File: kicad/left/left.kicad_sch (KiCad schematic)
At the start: 48 parts, among them J1 59453-121110ECHLF, J2 59453-051110ECHLF, J3 59453-051110ECHLF, J4 59453-081110EDHLF, J5 59453-081110EDHLF, U1 RP2040_Zero

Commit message: break up parts
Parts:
- removed D19, D20, D21, D22, D23, D24, D27, D28, D29, D30: D, ScottoKeebs_Components:Diode_SOD-123, symbol Device:D
- removed H4, H5: Mounting_Hole, MountingHole:MountingHole_2.2mm_M2_Pad_Via, symbol ScottoKeebs:Placeholder_Mounting_Hole
- removed J3: 59453-051110ECHLF, AMPHENOL_59453-051110ECHLF, symbol 59453-051110ECHLF:59453-051110ECHLF
- removed J4: 59453-081110EDHLF, AMPHENOL_59453-081110EDHLF, symbol 59453-081110EDHLF:59453-081110EDHLF
- removed S5, S6: SKRHADE010, SKRHADE010, symbol SKRHADE010:SKRHADE010
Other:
- moved on the sheet: H1, H2, H3, J1, J2, J5

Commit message: wiring
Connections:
- net GND: now also J2.5; no longer J2.4
- net JC: now also J2.4; no longer J2.3
- net JX: now also J2.3; no longer J2.5

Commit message: Add connectors
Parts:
- added J3: Conn_01x06_Pin, footprints:Pointing-connector, symbol Connector:Conn_01x06_Pin
- added J4: Conn_01x05_Pin, footprints:Joystick-connector, symbol Connector:Conn_01x05_Pin
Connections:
- net 3V3: now also J3.6 (Pin_6), J4.5 (Pin_5)
- net GND: now also J3.5 (Pin_5), J4.1 (Pin_1)
- net JC: now also J4.2 (Pin_2)
- net JX: now also J4.3 (Pin_3)
- net JY: now also J4.4 (Pin_4)
- net MISO: now also J3.2 (Pin_2)
- net MOSI: now also J3.4 (Pin_4)
- net SCK: now also J3.1 (Pin_1)
- net SS: now also J3.3 (Pin_3)

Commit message: Update footprints
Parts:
- H1, H2, H3: footprint MountingHole:MountingHole_2.2mm_M2_Pad_Via -> footprints:MountingHole_2.2mm_M2_Pad_Via
- J1: footprint AMPHENOL_59453-121110ECHLF -> footprints:AMPHENOL_59453-121110ECHLF
- J2: footprint AMPHENOL_59453-051110ECHLF -> footprints:AMPHENOL_59453-051110ECHLF
- J5: footprint AMPHENOL_59453-081110EDHLF -> footprints:AMPHENOL_59453-081110EDHLF
- S1, S2, S3, S4: footprint SKRHADE010 -> footprints:SKRHADE010
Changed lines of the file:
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@@
 			)
 		)
-		(property "Footprint" "SKRHADE010"
+		(property "Footprint" "footprints:SKRHADE010"
 			(at 59.69 143.18 0)
 			(effects
@@
 			)
 		)
-		(property "Footprint" "MountingHole:MountingHole_2.2mm_M2_Pad_Via"
+		(property "Footprint" "footprints:MountingHole_2.2mm_M2_Pad_Via"
 			(at 105.41 97.79 0)
 			(effects
@@
 			)
 		)
-		(property "Footprint" "SKRHADE010"
+		(property "Footprint" "footprints:SKRHADE010"
 			(at 129.54 143.18 0)
 			(effects
@@
 			)
 		)
-		(property "Footprint" "MountingHole:MountingHole_2.2mm_M2_Pad_Via"
+		(property "Footprint" "footprints:MountingHole_2.2mm_M2_Pad_Via"
 			(at 105.41 109.22 0)
 			(effects
@@
 			)
 		)
-		(property "Footprint" "SKRHADE010"
+		(property "Footprint" "footprints:SKRHADE010"
 			(at 199.39 143.18 0)
 			(effects
@@
 			)
 		)
-		(property "Footprint" "SKRHADE010"
+		(property "Footprint" "footprints:SKRHADE010"
 			(at 269.24 143.18 0)
 			(effects
@@
 			)
 		)
-		(property "Footprint" "MountingHole:MountingHole_2.2mm_M2_Pad_Via"
+		(property "Footprint" "footprints:MountingHole_2.2mm_M2_Pad_Via"
 			(at 105.41 104.14 0)
 			(effects
@@
 			)
 		)
-		(property "Footprint" "AMPHENOL_59453-051110ECHLF"
+		(property "Footprint" "footprints:AMPHENOL_59453-051110ECHLF"
 			(at 209.55 93.98 0)
 			(effects
@@
 			)
 		)
-		(property "Footprint" "AMPHENOL_59453-081110EDHLF"
+		(property "Footprint" "footprints:AMPHENOL_59453-081110EDHLF"
 			(at 254 92.71 0)
 			(effects
@@
 			)
 		)
-		(property "Footprint" "AMPHENOL_59453-121110ECHLF"
+		(property "Footprint" "footprints:AMPHENOL_59453-121110ECHLF"
 			(at 157.48 95.25 0)
 			(effects

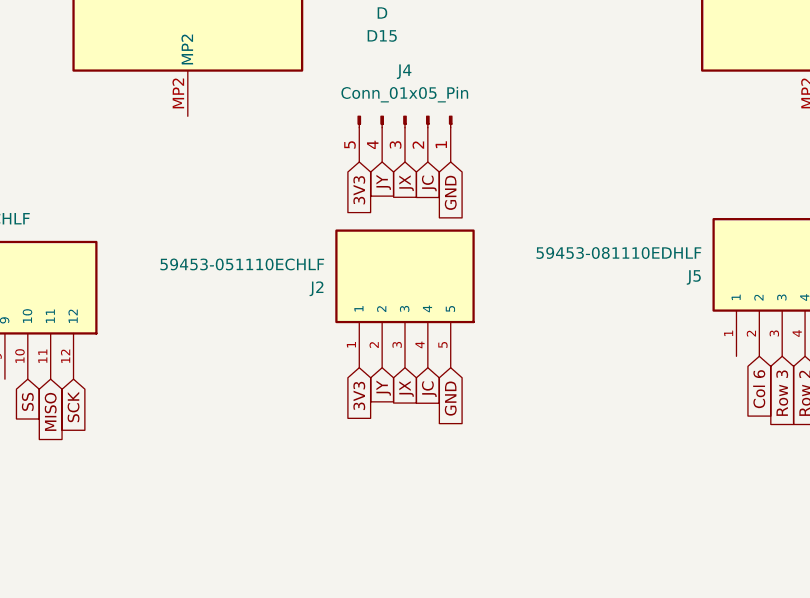
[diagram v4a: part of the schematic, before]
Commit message: Add joystick breakout
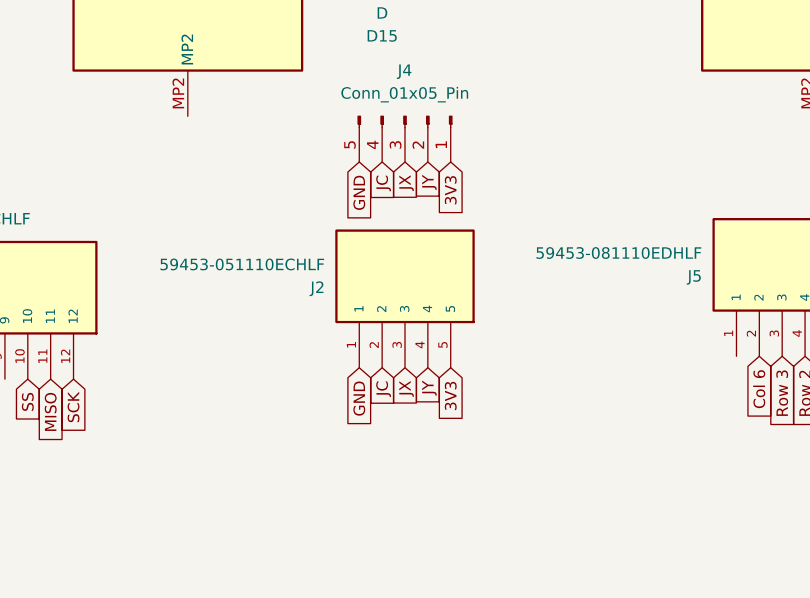
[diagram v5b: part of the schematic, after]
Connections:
- net 3V3: now also J2.5, J4.1 (Pin_1); no longer J2.1, J4.5 (Pin_5)
- net GND: now also J2.1, J4.5 (Pin_5); no longer J2.5, J4.1 (Pin_1)
- net JC: now also J2.2, J4.4 (Pin_4); no longer J2.4, J4.2 (Pin_2)
- net JY: now also J2.4, J4.2 (Pin_2); no longer J2.2, J4.4 (Pin_4)

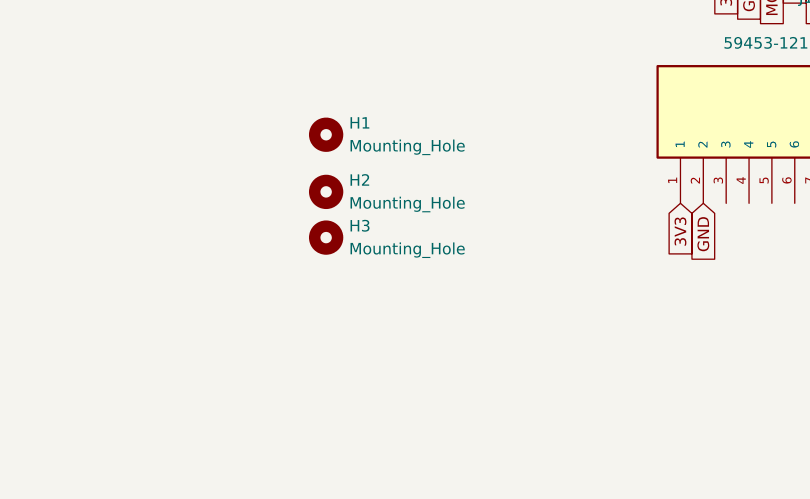
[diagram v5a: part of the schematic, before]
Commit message: Add holes
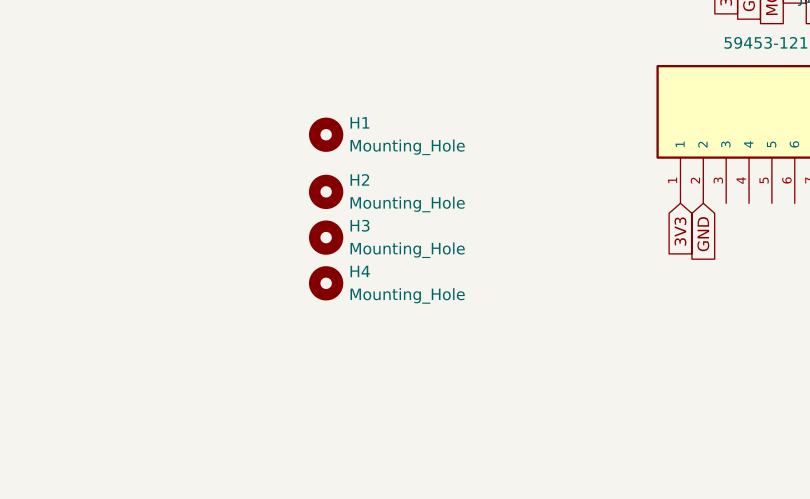
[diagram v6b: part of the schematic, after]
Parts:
- added H4: Mounting_Hole, footprints:MountingHole_2.2mm_M2_Pad_Via, symbol ScottoKeebs:Placeholder_Mounting_Hole
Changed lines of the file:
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@@
+	)
+	(symbol
+		(lib_id "ScottoKeebs:Placeholder_Mounting_Hole")
+		(at 105.41 114.3 0)
+		(unit 1)
+		(exclude_from_sim no)
+		(in_bom yes)
+		(on_board yes)
+		(dnp no)
+		(fields_autoplaced yes)
+		(property "Reference" "H4"
+			(at 107.95 113.0299 0)
+			(effects
+				(font
+					(size 1.27 1.27)
+				)
+				(justify left)
+			)
+		)
+		(property "Value" "Mounting_Hole"
+			(at 107.95 115.5699 0)
+			(effects
+				(font
+					(size 1.27 1.27)
+				)
+				(justify left)
+			)
+		)
+		(property "Footprint" "footprints:MountingHole_2.2mm_M2_Pad_Via"
+			(at 105.41 114.3 0)
+			(effects
+				(font
+					(size 1.27 1.27)
+				)
+				(hide yes)
+			)
+		)
+		(property "Datasheet" "~"
+			(at 105.41 114.3 0)
+			(effects
+				(font
+					(size 1.27 1.27)
+				)
+				(hide yes)
+			)
+		)
+		(property "Description" "Mounting Hole without connection"
+			(at 105.41 114.3 0)
+			(effects
+				(font
+					(size 1.27 1.27)
+				)
+				(hide yes)
+			)
+		)
+		(instances
+			(project "left"
+				(path "/feb70c3f-3e34-4f8f-9694-07d231f2d237"
+					(reference "H4")
+					(unit 1)
+				)
+			)
+		)
 	)
 	(symbol
